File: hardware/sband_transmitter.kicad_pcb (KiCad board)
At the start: 8 copper layers, 91.7 x 88.7 mm, 430 parts, among them IC1 LMS7002M, IC10 LM75, IC11 DAC6311IDCK, IC12 M24128, IC13 LD39100PUR, IC14 LMZ20501SILR, IC15 W25Q128JVSIQ, IC16 AD5662, IC17 AS431, IC18 LD39100PUR, IC2 M24128, IC20 74LVC1G3157FZ4, IC3 SKY13411-374LF, IC4 SKY13411-374LF, IC5 LD39100PUR, IC6 LD39100PUR, IC7 LFE5U-45F-MG285, IC9 LMK00105, J10 PC104-Mainboard, J11 Conn_Coaxial, J13 Conn_Coaxial, J3 FPGA GPIO, J4 FPGA EGPIO (board edge), J5 FPGA JTAG (board edge), J7 U.FL/MMCX, J8 U.FL/MMCX, J9 FAN, T1 TC1-1-13M-45+, T2 TC1-1-13M-45+, T3 TC1-1-13M-45+, T4 TC1-1-13M-45+, U2 GRF5115, U3 GRF5115

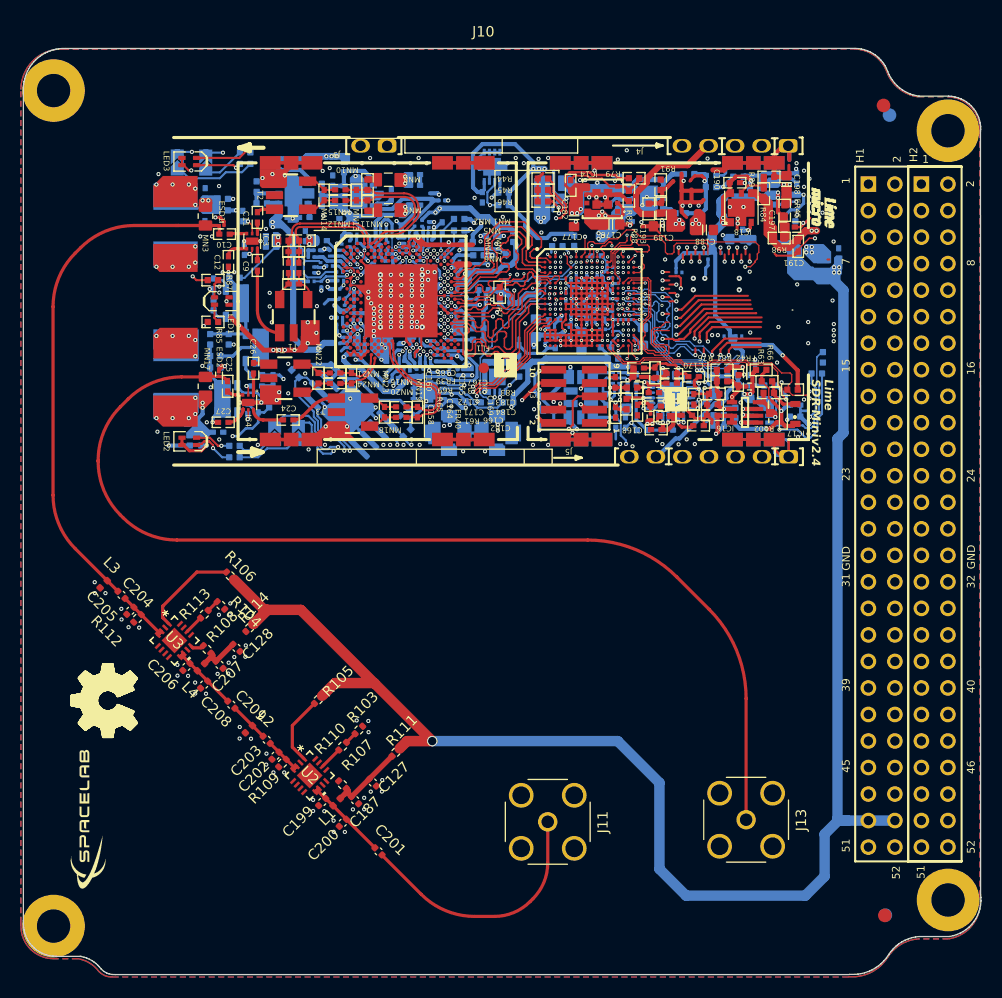
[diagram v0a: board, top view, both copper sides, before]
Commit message: Added RF Tools plugin for KiCAD v10, rerouted FPGA JTAG and FPGA EGPIO connectors and tracks, rerouted VCC5P0 track, added via fence around RF tracks.
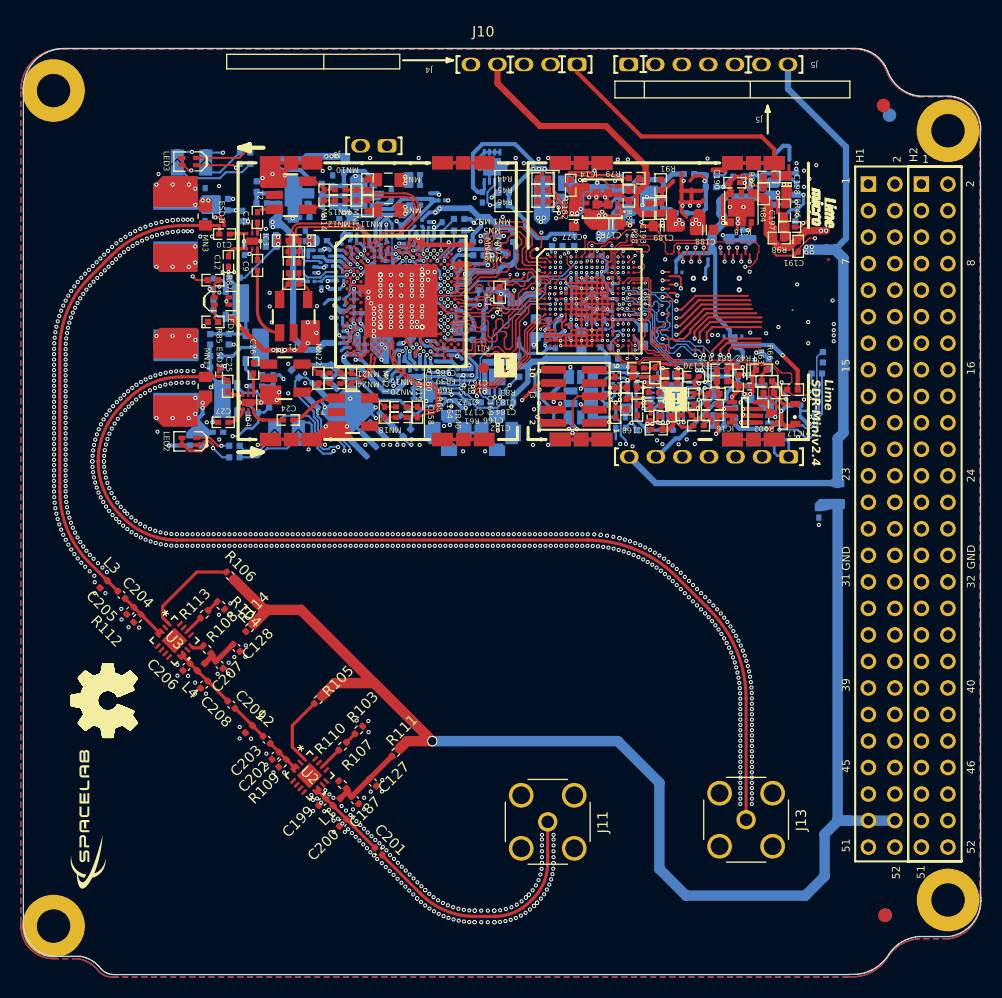
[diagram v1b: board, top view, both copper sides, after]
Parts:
- added J5: FPGA JTAG (board edge), LimeMicroAltiumLib_pcbLib:HEADER7X1_TH_V2, F.Cu at (167.2, 82.2)
- moved C133 24.9 mm to (177.8, 125.1), turned to -90 degrees
- moved J4 21.7 mm to (149.6, 82.2)
- moved FR36 21.5 mm to (179.6, 123.3)
- moved MECH10 19.0 mm to (105.1, 110.0)
- moved MECH1 8.07 mm to (170.2, 86.9), turned to 90 degrees
- moved R52 5.62 mm to (173.0, 110.9), turned to -90 degrees
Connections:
- IC7 pad A10: unconnected-(IC7A-PT27B/PCLKC0_1-PadA10) -> /08_FPGA/FPGA_EGPIO0
- J4 pad 1: unconnected-(J4-Pad1) -> GND
- U2 pad 5: unconnected-(U2-GND/NC-Pad5) -> GND
- U2 pad 6: unconnected-(U2-GND/NC-Pad6) -> GND
- U2 pad 7: unconnected-(U2-GND/NC-Pad7) -> GND
- U2 pad 8: unconnected-(U2-GND/NC-Pad8) -> GND
- U3 pad 5: unconnected-(U3-GND/NC-Pad5) -> GND
- U3 pad 6: unconnected-(U3-GND/NC-Pad6) -> GND
- U3 pad 7: unconnected-(U3-GND/NC-Pad7) -> GND
- U3 pad 8: unconnected-(U3-GND/NC-Pad8) -> GND
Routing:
- net /08_FPGA/FPGA_EGPIO0: track 0.00 -> 62.6 mm, vias 0 -> 1
- net /08_FPGA/FPGA_JTAG_TDO: track 32.7 -> 73.4 mm
- net /08_FPGA/FPGA_JTAG_TMS: track 33.3 -> 73.8 mm
- net /08_FPGA/FPGA_JTAG_TDI: track 33.7 -> 73.2 mm
- net (no net): track 1845.5 -> 1807.0 mm, vias 116 -> 115
- net VCC5P0: track 150.9 -> 180.0 mm
- net /08_FPGA/FPGA_EGPIO1: track 40.8 -> 64.3 mm
- net VCC_5V_RA_0: track 151.1 -> 128.1 mm, vias 5 -> 1
- net /08_FPGA/FPGA_JTAG_TCK: track 37.7 -> 60.6 mm
- net GND: track 471.1 -> 488.2 mm, vias 368 -> 1056
- net VCC3P3: track 238.4 -> 251.9 mm
- net TX: track 50.7 -> 47.3 mm
- net VCC2P5: track 75.0 -> 77.5 mm
